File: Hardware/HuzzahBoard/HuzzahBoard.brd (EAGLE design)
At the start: 76.2 x 50.5 mm, 2 parts, among them CN1 1X4-CLEANBIG

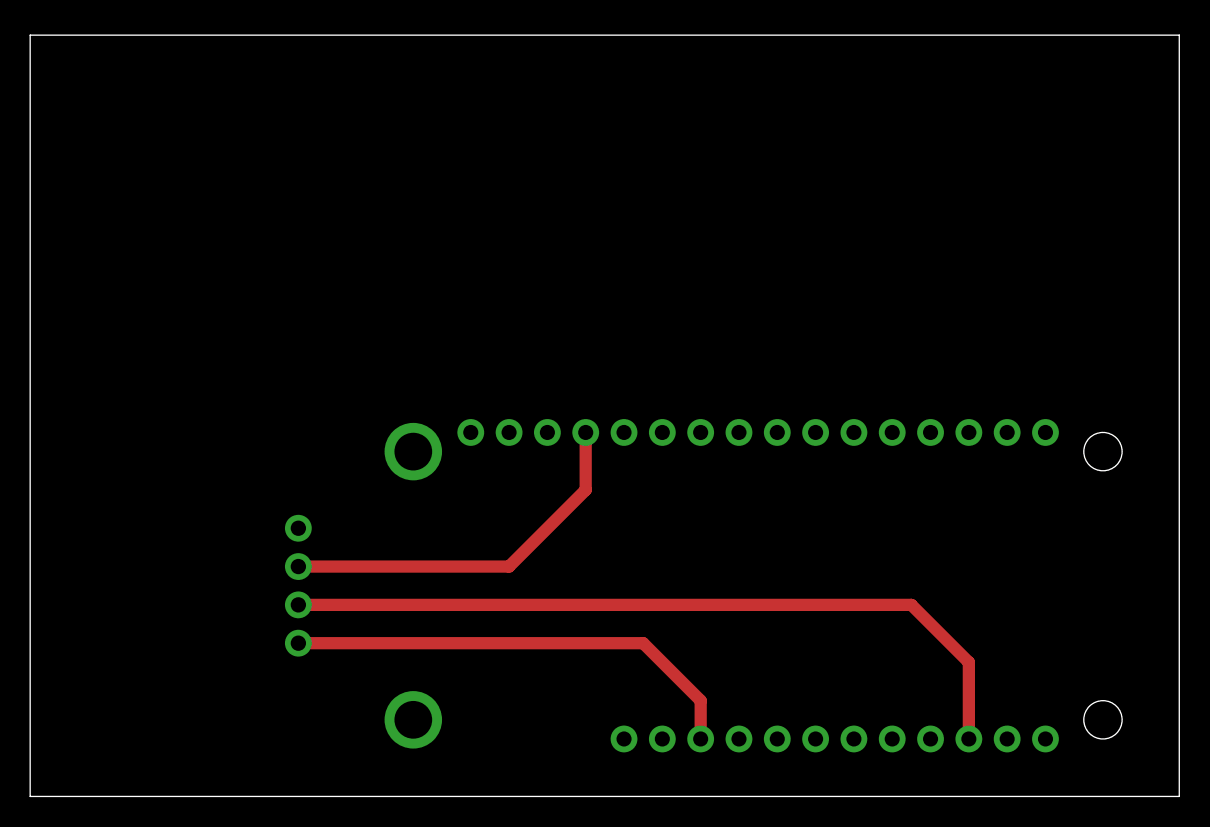
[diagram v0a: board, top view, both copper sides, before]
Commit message: board updates, move to bottom layer
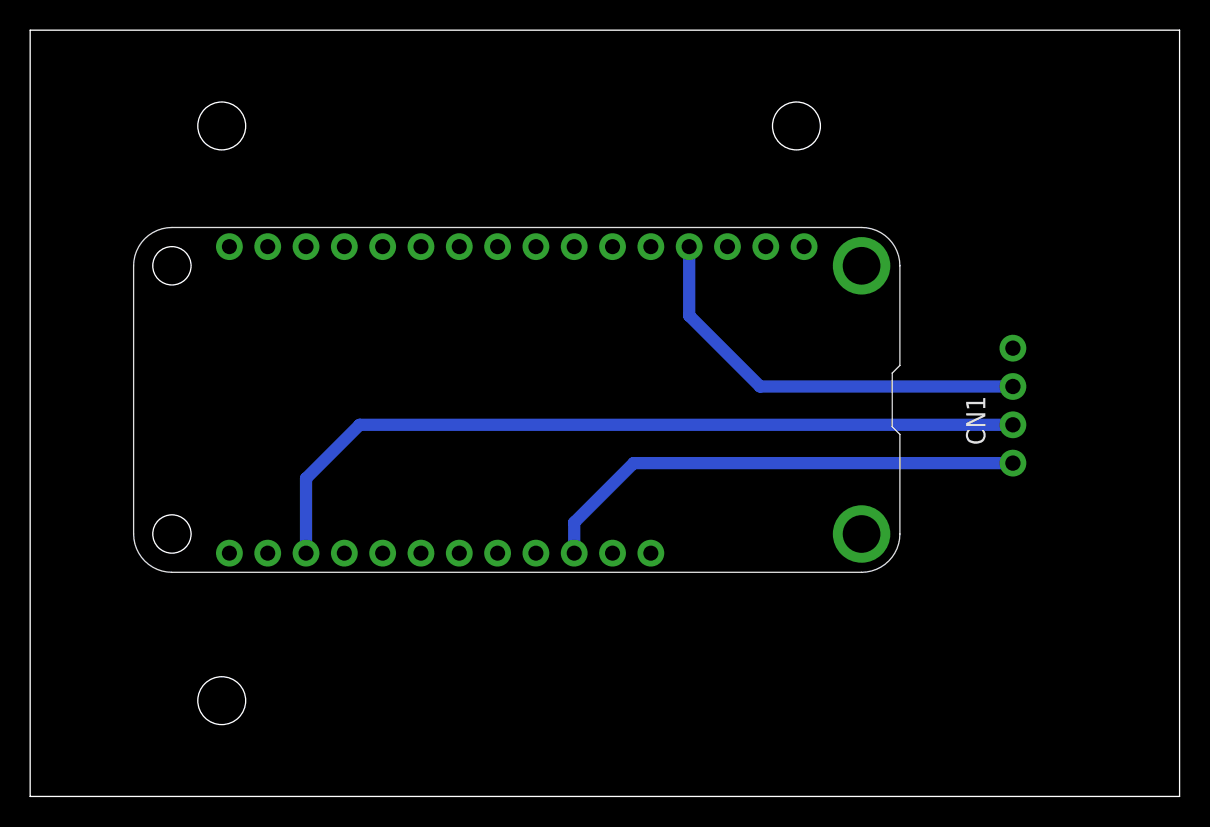
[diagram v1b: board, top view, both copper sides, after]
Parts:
- moved CN1 48.9 mm to (65.2, 25.9), flipped to the top
- moved MS1 36.9 mm to (57.7, 37.7), flipped to the top
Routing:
- net N$1: track 25.0 -> 28.0 mm
- net N$2: track 51.1 -> 53.3 mm
- net USB: track 30.8 -> 32.7 mm
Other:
- board size 76.2 x 50.5 mm -> 76.2 x 50.8 mm
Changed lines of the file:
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@@
 <setting verticaltext="up"/>
 </settings>
-<grid distance="50" unitdist="mil" unit="inch" style="dots" multiple="1" display="yes" altdistance="5" altunitdist="mil" altunit="inch"/>
+<grid distance="0.005" unitdist="inch" unit="inch" style="dots" multiple="1" display="yes" altdistance="5" altunitdist="mil" altunit="inch"/>
 <layers>
 <layer number="1" name="Top" color="4" fill="1" visible="yes" active="yes"/>
@@
 <layer number="43" name="vRestrict" color="2" fill="10" visible="yes" active="yes"/>
 <layer number="44" name="Drills" color="7" fill="1" visible="no" active="yes"/>
-<layer number="45" name="Holes" color="7" fill="1" visible="no" active="yes"/>
+<layer number="45" name="Holes" color="7" fill="1" visible="yes" active="yes"/>
 <layer number="46" name="Milling" color="3" fill="1" visible="no" active="yes"/>
 <layer number="47" name="Measures" color="7" fill="1" visible="no" active="yes"/>
@@
 <board>
 <plain>
-<wire x1="0" y1="0" x2="76.18" y2="0" width="0" layer="20"/>
-<wire x1="76.18" y1="0" x2="76.18" y2="50.47" width="0" layer="20"/>
-<wire x1="76.18" y1="50.47" x2="0" y2="50.47" width="0" layer="20"/>
-<wire x1="0" y1="50.47" x2="0" y2="0" width="0" layer="20"/>
-<dimension x1="0" y1="0" x2="76.2" y2="0" x3="38.1" y3="-10.16" textsize="1.778" layer="1" unit="inch"/>
-<dimension x1="0" y1="0" x2="0" y2="50.8" x3="-12.7" y3="25.4" textsize="1.778" layer="1" unit="inch"/>
+<wire x1="0" y1="0" x2="76.2" y2="0" width="0" layer="20"/>
+<wire x1="76.2" y1="0" x2="76.2" y2="50.8" width="0" layer="20"/>
+<wire x1="76.2" y1="50.8" x2="0" y2="50.8" width="0" layer="20"/>
+<wire x1="0" y1="50.8" x2="0" y2="0" width="0" layer="20"/>
+<hole x="12.7" y="44.45" drill="3.175"/>
+<hole x="50.8" y="44.45" drill="3.175"/>
+<hole x="12.7" y="6.35" drill="3.175"/>
 </plain>
 <attributes>
@@
 </class>
 </classes>
-<designrules name="default">
-<description language="de">&lt;b&gt;EAGLE Design Rules&lt;/b&gt;
-&lt;p&gt;
-Die Standard-Design-Rules sind so gewählt, dass sie für
-die meisten Anwendungen passen. Sollte ihre Platine
-besondere Anforderungen haben, treffen Sie die erforderlichen
-Einstellungen hier und speichern die Design Rules unter
-einem neuen Namen ab.</description>
-<description language="en">&lt;b&gt;EAGLE Design Rules&lt;/b&gt;
-&lt;p&gt;
-The default Design Rules have been set to cover
-a wide range of applications. Your particular design
-may have different requirements, so please make the
-necessary adjustments and save your customized
-design rules under a new name.</description>
+<designrules name="OthermillDRC_1_64_v2">
+<description language="en">&lt;b&gt;Othermill EAGLE Design Rules v2&lt;/b&gt;&lt;p&gt;DRC for Othermill, 1/64&quot; tool&lt;/p&gt;&lt;b&gt;-- Rules --&lt;/b&gt;&lt;li&gt;8 mil traces&lt;/li&gt;&lt;li&gt;15.7mil clearance&lt;/li&gt;</description>
 <param name="layerSetup" value="(1*16)"/>
 <param name="mtCopper" value="0.035mm 0.035mm 0.035mm 0.035mm 0.035mm 0.035mm 0.035mm 0.035mm 0.035mm 0.035mm 0.035mm 0.035mm 0.035mm 0.035mm 0.035mm 0.035mm"/>
 <param name="mtIsolate" value="1.5mm 0.15mm 0.2mm 0.15mm 0.2mm 0.15mm 0.2mm 0.15mm 0.2mm 0.15mm 0.2mm 0.15mm 0.2mm 0.15mm 0.2mm"/>
-<param name="mdWireWire" value="6mil"/>
-<param name="mdWirePad" value="6mil"/>
-<param name="mdWireVia" value="6mil"/>
-<param name="mdPadPad" value="6mil"/>
-<param name="mdPadVia" value="6mil"/>
-<param name="mdViaVia" value="6mil"/>
-<param name="mdSmdPad" value="6mil"/>
-<param name="mdSmdVia" value="6mil"/>
-<param name="mdSmdSmd" value="6mil"/>
-<param name="mdViaViaSameLayer" value="6mil"/>
+<param name="mdWireWire" value="0.39878125mm"/>
+<param name="mdWirePad" value="0.39878125mm"/>
+<param name="mdWireVia" value="0.39878125mm"/>
+<param name="mdPadPad" value="0.39878125mm"/>
+<param name="mdPadVia" value="0.39878125mm"/>
+<param name="mdViaVia" value="0.39878125mm"/>
+<param name="mdSmdPad" value="0mil"/>
+<param name="mdSmdVia" value="0mil"/>
+<param name="mdSmdSmd" value="0mil"/>
+<param name="mdViaViaSameLayer" value="8mil"/>
 <param name="mnLayersViaInSmd" value="2"/>
-<param name="mdCopperDimension" value="40mil"/>
-<param name="mdDrill" value="6mil"/>
+<param name="mdCopperDimension" value="0mil"/>
+<param name="mdDrill" value="1mil"/>
 <param name="mdSmdStop" value="0mil"/>
-<param name="msWidth" value="6mil"/>
-<param name="msDrill" value="0.35mm"/>
+<param name="msWidth" value="16mil"/>
+<param name="msDrill" value="31mil"/>
 <param name="msMicroVia" value="9.99mm"/>
 <param name="msBlindViaRatio" value="0.5"/>
@@
 <param name="rvMicroViaOuter" value="0.25"/>
 <param name="rvMicroViaInner" value="0.25"/>
-<param name="rlMinPadTop" value="10mil"/>
-<param name="rlMaxPadTop" value="20mil"/>
-<param name="rlMinPadInner" value="10mil"/>
-<param name="rlMaxPadInner" value="20mil"/>
-<param name="rlMinPadBottom" value="10mil"/>
-<param name="rlMaxPadBottom" value="20mil"/>
-<param name="rlMinViaOuter" value="8mil"/>
-<param name="rlMaxViaOuter" value="20mil"/>
+<param name="rlMinPadTop" value="0mil"/>
+<param name="rlMaxPadTop" value="9999mil"/>
+<param name="rlMinPadInner" value="0mil"/>
+<param name="rlMaxPadInner" value="9999mil"/>
+<param name="rlMinPadBottom" value="0mil"/>
+<param name="rlMaxPadBottom" value="9999mil"/>
+<param name="rlMinViaOuter" value="15mil"/>
+<param name="rlMaxViaOuter" value="25mil"/>
 <param name="rlMinViaInner" value="8mil"/>
-<param name="rlMaxViaInner" value="20mil"/>
+<param name="rlMaxViaInner" value="25mil"/>
 <param name="rlMinMicroViaOuter" value="4mil"/>
 <param name="rlMaxMicroViaOuter" value="20mil"/>
@@
 <param name="psBottom" value="-1"/>
 <param name="psFirst" value="-1"/>
-<param name="psElongationLong" value="100"/>
+<param name="psElongationLong" value="50"/>
 <param name="psElongationOffset" value="100"/>
-<param name="mvStopFrame" value="1"/>
-<param name="mvCreamFrame" value="0"/>
-<param name="mlMinStopFrame" value="4mil"/>
-<param name="mlMaxStopFrame" value="4mil"/>
-<param name="mlMinCreamFrame" value="0mil"/>
-<param name="mlMaxCreamFrame" value="0mil"/>
-<param name="mlViaStopLimit" value="0mil"/>
-<param name="srRoundness" value="0"/>
-<param name="srMinRoundness" value="0mil"/>
-<param name="srMaxRoundness" value="0mil"/>
+<param name="mvStopFrame" value="0.05"/>
+<param name="mvCreamFrame" value="0.05"/>
+<param name="mlMinStopFrame" value="1mil"/>
+<param name="mlMaxStopFrame" value="2mil"/>
+<param name="mlMinCreamFrame" value="2mil"/>
+<param name="mlMaxCreamFrame" value="10mil"/>
+<param name="mlViaStopLimit" value="30mil"/>
+<param name="srRoundness" value="0.1"/>
+<param name="srMinRoundness" value="2mil"/>
+<param name="srMaxRoundness" value="10mil"/>
 <param name="slThermalIsolate" value="10mil"/>
 <param name="slThermalsForVias" value="0"/>
@@
 </autorouter>
 <elements>
-<element name="CN1" library="adafruit" package="1X04-CLEANBIG" value="1X4-CLEANBIG" x="17.78" y="13.97" rot="MR90"/>
-<element name="MS1" library="adafruit" package="FEATHERWING_DIM" value="FEATHERWING_NODIM" x="22.86" y="25.4" rot="MR180"/>
+<element name="CN1" library="adafruit" package="1X04-CLEANBIG" value="1X4-CLEANBIG" x="65.151" y="25.908" rot="R90"/>
+<element name="MS1" library="adafruit" package="FEATHERWING_DIM" value="FEATHERWING_NODIM" x="57.658" y="37.719" rot="R180"/>
 </elements>
 <signals>
@@
 <contactref element="MS1" pad="26"/>
 <contactref element="CN1" pad="1"/>
-<wire x1="17.78" y1="10.16" x2="40.64" y2="10.16" width="0.8128" layer="1"/>
-<wire x1="40.64" y1="10.16" x2="44.45" y2="6.35" width="0.8128" layer="1"/>
-<wire x1="44.45" y1="6.35" x2="44.45" y2="3.81" width="0.8128" layer="1"/>
+<wire x1="36.068" y1="16.129" x2="36.068" y2="18.161" width="0.8128" layer="16"/>
+<wire x1="36.068" y1="18.161" x2="40.005" y2="22.098" width="0.8128" layer="16"/>
+<wire x1="40.005" y1="22.098" x2="65.151" y2="22.098" width="0.8128" layer="16"/>
 </signal>
 <signal name="N$1">
 <contactref element="MS1" pad="4"/>
 <contactref element="CN1" pad="3"/>
-<wire x1="17.78" y1="15.24" x2="31.75" y2="15.24" width="0.8128" layer="1"/>
-<wire x1="31.75" y1="15.24" x2="36.83" y2="20.32" width="0.8128" layer="1"/>
-<wire x1="36.83" y1="20.32" x2="36.83" y2="24.13" width="0.8128" layer="1"/>
+<wire x1="43.688" y1="36.449" x2="43.688" y2="31.877" width="0.8128" layer="16"/>
+<wire x1="43.688" y1="31.877" x2="48.387" y2="27.178" width="0.8128" layer="16"/>
+<wire x1="48.387" y1="27.178" x2="65.151" y2="27.178" width="0.8128" layer="16"/>
 </signal>
 <signal name="N$2">
 <contactref element="MS1" pad="19"/>
 <contactref element="CN1" pad="2"/>
-<wire x1="17.78" y1="12.7" x2="58.42" y2="12.7" width="0.8128" layer="1"/>
-<wire x1="58.42" y1="12.7" x2="62.23" y2="8.89" width="0.8128" layer="1"/>
-<wire x1="62.23" y1="8.89" x2="62.23" y2="3.81" width="0.8128" layer="1"/>
+<wire x1="18.288" y1="16.129" x2="18.288" y2="21.082" width="0.8128" layer="16"/>
+<wire x1="18.288" y1="21.082" x2="21.844" y2="24.638" width="0.8128" layer="16"/>
+<wire x1="21.844" y1="24.638" x2="65.151" y2="24.638" width="0.8128" layer="16"/>
 </signal>
 </signals>

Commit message: revise board layout
WIre Colors for Servo: ORB - PWM, VCC, GROUND
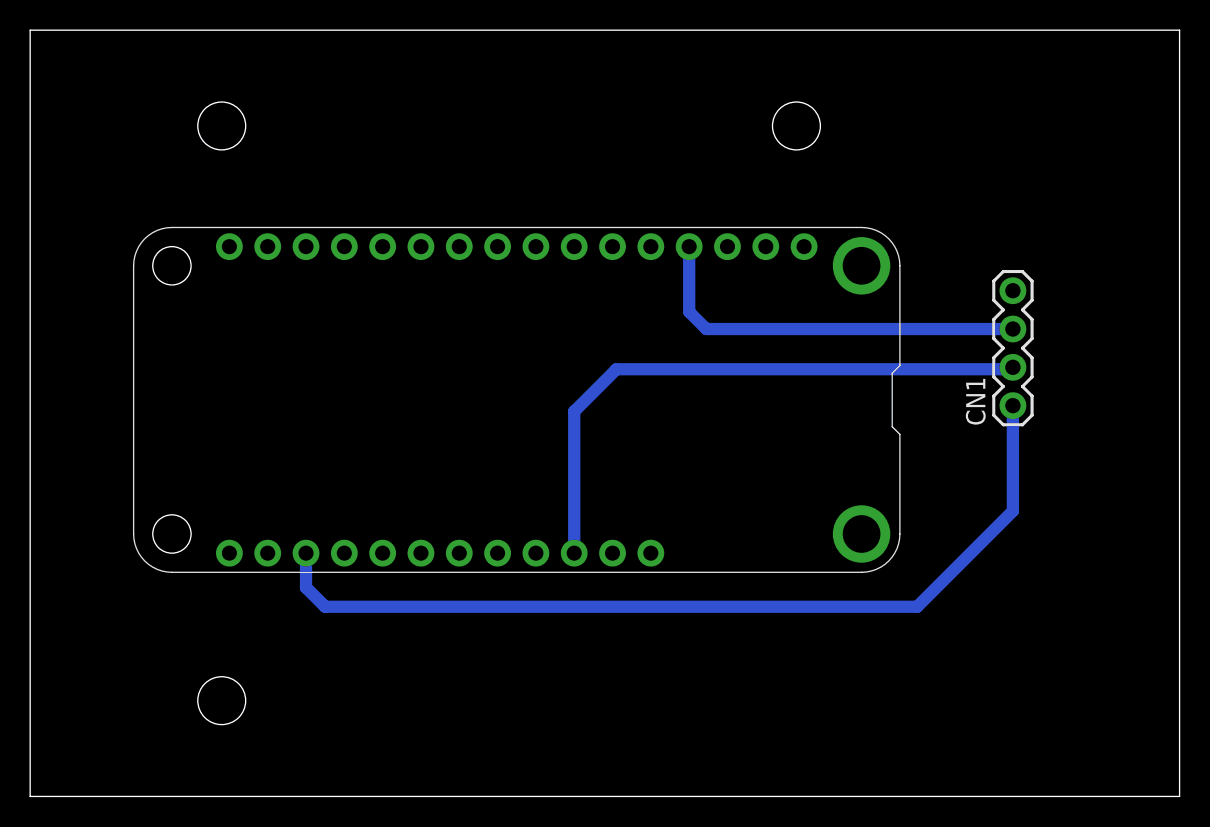
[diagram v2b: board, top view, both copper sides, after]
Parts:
- CN1: value 1X4-CLEANBIG -> 1X4-BIG; device adafruit:1X04-CLEANBIG -> adafruit:1X04-BIG
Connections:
- net N$1 renamed GND
- removed net N$2: CN1.2, MS1.19
- new net GPIO5_PWM: CN1.1, MS1.19
- net USB: now also CN1.2; no longer CN1.1
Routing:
- net GPIO5_PWM: track 0.00 -> 59.3 mm
- net N$2: track 53.3 -> 0.00 mm
- net USB: track 32.7 -> 39.7 mm
- net GND: track 28.0 -> 26.3 mm
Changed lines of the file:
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@@
 </autorouter>
 <elements>
-<element name="CN1" library="adafruit" package="1X04-CLEANBIG" value="1X4-CLEANBIG" x="65.151" y="25.908" rot="R90"/>
+<element name="CN1" library="adafruit" package="1X04-BIG" value="1X4-BIG" x="65.151" y="25.908" rot="R90"/>
 <element name="MS1" library="adafruit" package="FEATHERWING_DIM" value="FEATHERWING_NODIM" x="57.658" y="37.719" rot="R180"/>
 </elements>
 <signals>
+<signal name="GPIO5_PWM">
+<contactref element="MS1" pad="19"/>
+<contactref element="CN1" pad="1"/>
+<wire x1="18.288" y1="16.129" x2="18.288" y2="13.843" width="0.8128" layer="16"/>
+<wire x1="18.288" y1="13.843" x2="19.558" y2="12.573" width="0.8128" layer="16"/>
+<wire x1="19.558" y1="12.573" x2="58.801" y2="12.573" width="0.8128" layer="16"/>
+<wire x1="58.801" y1="12.573" x2="65.151" y2="18.923" width="0.8128" layer="16"/>
+<wire x1="65.151" y1="18.923" x2="65.151" y2="25.908" width="0.8128" layer="16"/>
+</signal>
 <signal name="USB">
 <contactref element="MS1" pad="26"/>
-<contactref element="CN1" pad="1"/>
-<wire x1="36.068" y1="16.129" x2="36.068" y2="18.161" width="0.8128" layer="16"/>
-<wire x1="36.068" y1="18.161" x2="40.005" y2="22.098" width="0.8128" layer="16"/>
-<wire x1="40.005" y1="22.098" x2="65.151" y2="22.098" width="0.8128" layer="16"/>
+<contactref element="CN1" pad="2"/>
+<wire x1="36.068" y1="16.129" x2="36.068" y2="25.527" width="0.8128" layer="16"/>
+<wire x1="36.068" y1="25.527" x2="38.862" y2="28.321" width="0.8128" layer="16"/>
+<wire x1="38.862" y1="28.321" x2="65.024" y2="28.321" width="0.8128" layer="16"/>
+<wire x1="65.024" y1="28.321" x2="65.151" y2="28.448" width="0.8128" layer="16"/>
 </signal>
-<signal name="N$1">
+<signal name="GND">
 <contactref element="MS1" pad="4"/>
 <contactref element="CN1" pad="3"/>
-<wire x1="43.688" y1="36.449" x2="43.688" y2="31.877" width="0.8128" layer="16"/>
-<wire x1="43.688" y1="31.877" x2="48.387" y2="27.178" width="0.8128" layer="16"/>
-<wire x1="48.387" y1="27.178" x2="65.151" y2="27.178" width="0.8128" layer="16"/>
-</signal>
-<signal name="N$2">
-<contactref element="MS1" pad="19"/>
-<contactref element="CN1" pad="2"/>
-<wire x1="18.288" y1="16.129" x2="18.288" y2="21.082" width="0.8128" layer="16"/>
-<wire x1="18.288" y1="21.082" x2="21.844" y2="24.638" width="0.8128" layer="16"/>
-<wire x1="21.844" y1="24.638" x2="65.151" y2="24.638" width="0.8128" layer="16"/>
+<wire x1="43.688" y1="36.449" x2="43.688" y2="32.131" width="0.8128" layer="16"/>
+<wire x1="43.688" y1="32.131" x2="44.831" y2="30.988" width="0.8128" layer="16"/>
+<wire x1="44.831" y1="30.988" x2="65.151" y2="30.988" width="0.8128" layer="16"/>
 </signal>
 </signals>
